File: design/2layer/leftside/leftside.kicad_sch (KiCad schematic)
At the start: 236 parts, among them IC2 MCP23009-E_MG, IC3 nRF52833-QDAA-R7, IC5 XCL110A503KR-G, IC6 TPS22917LDBVT, IC7 SN74AHCT1G125DCKR, IC8 TPS63051RMWT, J1 USB_C_Receptacle_USB2.0_16P, J2 Battery+, J3 Battery-, J4 OLED_128x32, J5 Conn_01x01, J6 Conn_01x04, J7 F32Q-1A7H1-11012, J8 Conn_01x01, U1 BQ27441-G1, U2 BQ24072RGT, U3 USB6B1, U5 PEC11L-4015F-S0015, Y1 ECS-320-8-37B2-JTY-TR

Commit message: Replaced TPS63051 with TPS63031 as out of stock
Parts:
- removed IC8: TPS63051RMWT, QFN50P250X250X100-12N-D, symbol SamacSys:TPS63051RMWT
- removed PG1: TestPoint, TestPoint:TestPoint_Pad_D1.0mm, symbol Connector:TestPoint
- added IC4: TPS63031DSKT, SON50P250X250X80-11N-D, symbol SamacSys:TPS63031DSKT
- PC1: value 10uF -> 100nF
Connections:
- net 3V3: now also PC3.2, PC47.2, IC4.1 (VOUT), IC4.10 (FB); no longer PC1.1, PC27.1
- net GND: now also PC1.1, PC27.1, PC3.1, PC47.1, IC4.11 (EP), IC4.3 (PGND), IC4.7 (PS/SYNC), IC4.9 (GND); no longer PC1.2, PC27.2, PC3.2, PC47.2
- net at IC5.1 (1/VIN), IC5.3 (3/EN), IC5.7 (7/L1)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: now also PC1.2, PC27.2, IC4.5 (VIN), IC4.6 (EN), IC4.8 (VINA); no longer PC3.1, PC47.1
- net at PL5.2: now also IC4.2 (L2)
- net at PL5.1: now also IC4.4 (L1)
- no-connect marks 18 -> 17
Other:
- moved on the sheet: IC5, PC25, PC26

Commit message: Create blender model + PCB review fixes
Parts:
- removed C29, C39, C4, C45: 100nF, ScottoKeebs_Components:Capacitor_0603, symbol Device:C_Small
- removed C44: 10uF, ScottoKeebs_Components:Capacitor_0603, symbol Device:C_Small
- removed PL5: 1.5uH, Inductor_SMD:L_0603_1608Metric, symbol Device:L_Small
- added C46, PC28: 100nF, ScottoKeebs_Components:Capacitor_0603, symbol Device:C_Small
- added PC29: 10uF, ScottoKeebs_Components:Capacitor_0603, symbol Device:C_Small
- added PL1: LPS3015-153MRC, Snapeda:IND_LPS3015-153MRC, symbol Device:L
- added SR17, SR18: 47, Resistor_SMD:R_0603_1608Metric, symbol Device:R
- added SR6: 100k, Resistor_SMD:R_0603_1608Metric, symbol Device:R
- C2, C21, C28, C3, C30, C31, C32, C33, C35, C36, C38, C41, C42, C43: value 100nF -> 10uF
- F1: value 6A -> .75A
- PR3: value 1k8 -> 2k2
- SC10: value 10nF -> 0nF(10)
- SR4: value 4k7 -> 100k
- renumbered PL4 to SL4
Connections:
- net 5V: now also C46.1, PC29.2
- net GND: now also C46.2, PC28.2, PC29.1, SR6.1
- net Row 0: now also Di1.2 (A), Di12.2 (A), Di16.2 (A), Di24.2 (A), Di7.2 (A); no longer Di1.1 (K), Di12.1 (K), Di16.1 (K), Di24.1 (K), Di7.1 (K)
- net Row 1: now also Di10.2 (A), Di2.2 (A), Di26.2 (A), Di8.2 (A), Di9.2 (A); no longer Di10.1 (K), Di2.1 (K), Di26.1 (K), Di8.1 (K), Di9.1 (K)
- net Row 2: now also Di13.2 (A), Di14.2 (A), Di15.2 (A), Di27.2 (A), Di3.2 (A); no longer Di13.1 (K), Di14.1 (K), Di15.1 (K), Di27.1 (K), Di3.1 (K)
- net Row 3: now also Di18.2 (A), Di19.2 (A), Di21.2 (A), Di28.2 (A), Di5.2 (A); no longer Di18.1 (K), Di19.1 (K), Di21.1 (K), Di28.1 (K), Di5.1 (K)
- net Row 4: now also Di17.2 (A), Di22.2 (A), Di23.2 (A), Di29.2 (A), Di6.2 (A); no longer Di17.1 (K), Di22.1 (K), Di23.1 (K), Di29.1 (K), Di6.1 (K)
- net Row 5: now also Di11.2 (A), Di20.2 (A), Di25.2 (A), Di30.2 (A), Di4.2 (A), IC2.9 (GP0); no longer Di11.1 (K), Di20.1 (K), Di25.1 (K), Di30.1 (K), Di4.1 (K), IC2.10 (GP1)
- net Row 6: now also Di36.2 (A), IC2.10 (GP1); no longer Di36.1 (K), IC2.11 (GP2)
- net SCL: now also SR17.2; no longer IC3.2 (P0.00)
- net SDA: now also SR18.2; no longer IC3.3 (P0.01)
- net VBUS: now also PC28.1
- net at S4.2: now also Di16.1 (K); no longer Di16.2 (A)
- net at S11.2: now also Di3.1 (K); no longer Di3.2 (A)
- net at IC4.5 (VIN), IC4.6 (EN), IC4.8 (VINA)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: no longer IC5.3 (3/EN)
- net at S22.2: now also Di6.1 (K); no longer Di6.2 (A)
- net at S6.2: now also Di8.1 (K); no longer Di8.2 (A)
- net at S23.2: now also Di22.1 (K); no longer Di22.2 (A)
- net at S19.2: now also Di19.1 (K); no longer Di19.2 (A)
- net at S8.2: now also Di2.1 (K); no longer Di2.2 (A)
- net at S2.2: now also Di7.1 (K); no longer Di7.2 (A)
- net at IC4.4 (L1): now also PL1.1
- net at IC4.2 (L2): now also PL1.2
- net at S17.2: now also Di18.1 (K); no longer Di18.2 (A)
- net at S26.2: now also Di11.1 (K); no longer Di11.2 (A)
- net at S35.2: now also Di36.1 (K); no longer Di36.2 (A)
- net at S29.2: now also Di25.1 (K); no longer Di25.2 (A)
- net at S14.2: now also Di15.1 (K); no longer Di15.2 (A)
- net at S13.2: now also Di14.1 (K); no longer Di14.2 (A)
- net at S24.2: now also Di23.1 (K); no longer Di23.2 (A)
- net at S3.2: now also Di12.1 (K); no longer Di12.2 (A)
- net at S28.2: now also Di20.1 (K); no longer Di20.2 (A)
- net at S9.2: now also Di10.1 (K); no longer Di10.2 (A)
- net at S30.2: now also Di30.1 (K); no longer Di30.2 (A)
- net at S1.2: now also Di1.1 (K); no longer Di1.2 (A)
- net at S10.2: now also Di26.1 (K); no longer Di26.2 (A)
- net at S12.2: now also Di13.1 (K); no longer Di13.2 (A)
- net at S25.2: now also Di29.1 (K); no longer Di29.2 (A)
- net at S18.2: now also Di5.1 (K); no longer Di5.2 (A)
- net at S5.2: now also Di24.1 (K); no longer Di24.2 (A)
- net at S7.2: now also Di9.1 (K); no longer Di9.2 (A)
- net at S20.2: now also Di28.1 (K); no longer Di28.2 (A)
- net at S27.2: now also Di4.1 (K); no longer Di4.2 (A)
- net at S15.2: now also Di27.1 (K); no longer Di27.2 (A)
- net at S21.2: now also Di17.1 (K); no longer Di17.2 (A)
- net at S16.2: now also Di21.1 (K); no longer Di21.2 (A)
- new net: IC3.3 (P0.01), SR18.1
- new net: IC3.2 (P0.00), SR17.1
- new net 5VEN: IC2.11 (GP2), IC5.3 (3/EN), SR6.2
- no-connect marks 17 -> 16
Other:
- note added: "Address: 0x55 (85)"
- note added: "BLE Enabled - QFN40 Config 5"
- note added: "Battery charging and USB power stage. ILIM controls input current limit calculated by 1550/R = limit. 3k = 500mA | 2k2 = 705mA ISET controls battery current charge limit calculated by 890/R = limit. 1.8k = 500mA | 1k = 890mA White LED for charging status with CHG. TPS2291 load switch for better stability when turning on/off. White LED for USB Power connection Optional film NTC thermistor for batt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"
- note removed: "BLE Enabled - QFN40 Config 3"
- note removed: "Battery charging and USB power stage. Output 3.3V. ILIM controls input current limit calculated by 1550/R = limit. 3k = 500mA | 1k8 = 860mA ISET controls battery current charge limit calculated by 890/R = limit. 1.8k = 500mA | 1k = 890mA White LED for charging status with CHG. TPS2291 load switch for better stability when turning on/off. White LED for USB Power connection Optional film NTC thermi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"
- moved on the sheet: Di1, Di10, Di11, Di12, Di13, Di14, Di15, Di16, Di17, Di18, Di19, Di2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

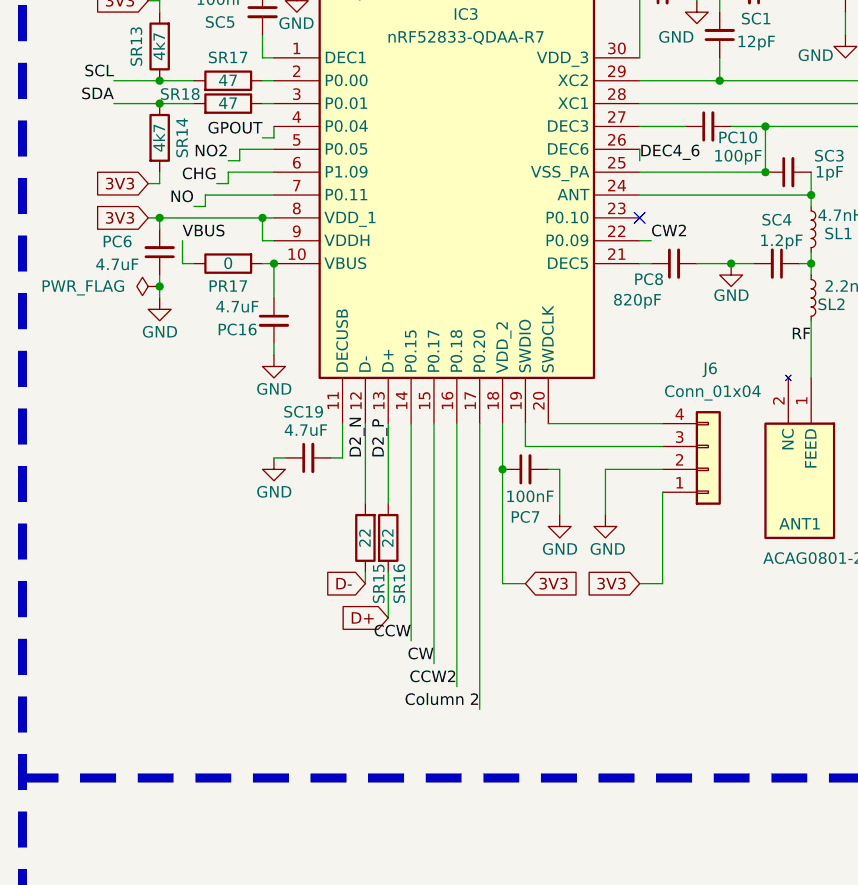
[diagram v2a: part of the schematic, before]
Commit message: Add keyboard render
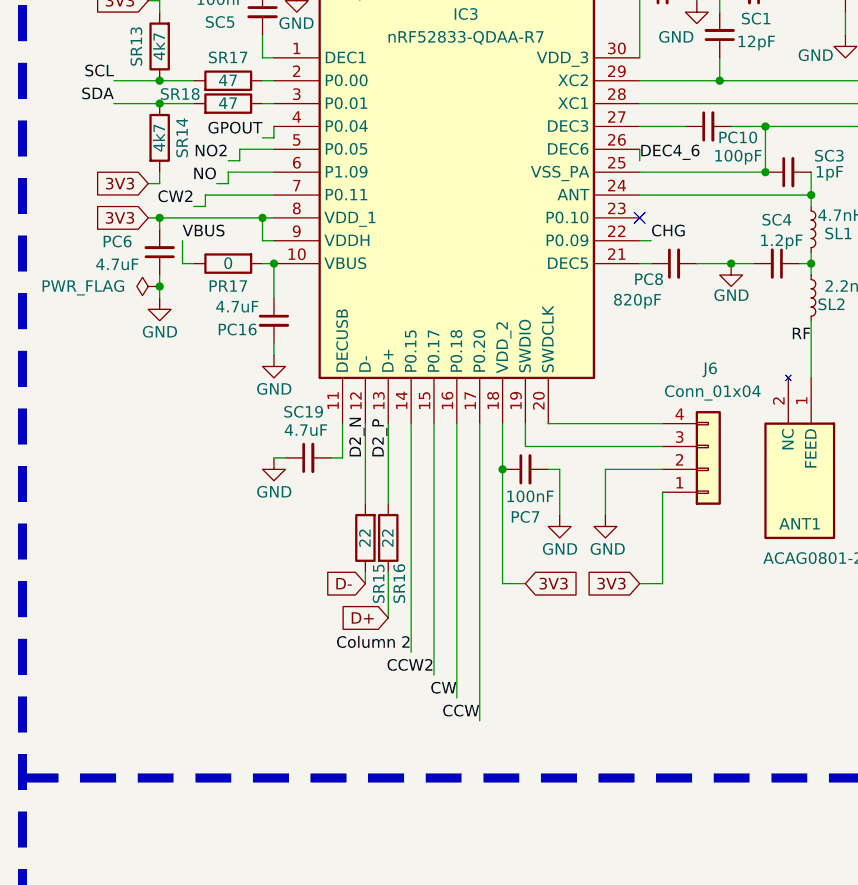
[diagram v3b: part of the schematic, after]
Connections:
- net CCW: now also IC3.17 (P0.20); no longer IC3.14 (P0.15)
- net CCW2: now also IC3.15 (P0.17); no longer IC3.16 (P0.18)
- net CHG: now also IC3.22 (P0.09); no longer IC3.6 (P1.09)
- net CW: now also IC3.16 (P0.18); no longer IC3.15 (P0.17)
- net CW2: now also IC3.7 (P0.11); no longer IC3.22 (P0.09)
- net Column 2: now also IC3.14 (P0.15); no longer IC3.17 (P0.20)
- net NO: now also IC3.6 (P1.09); no longer IC3.7 (P0.11)
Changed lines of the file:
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@@
 	(wire
 		(pts
-			(xy 59.69 124.46) (xy 59.69 151.13)
-		)
-		(stroke
-			(width 0)
-			(type default)
-		)
-	)
-	(wire
-		(pts
 			(xy 80.01 264.16) (xy 80.01 259.08)
 		)
@@
 	(wire
 		(pts
-			(xy 62.23 124.46) (xy 62.23 153.67)
-		)
-		(stroke
-			(width 0)
-			(type default)
-		)
-	)
-	(wire
-		(pts
 			(xy 554.99 137.16) (xy 551.18 137.16)
 		)
@@
 	(wire
 		(pts
-			(xy 64.77 124.46) (xy 64.77 156.21)
+			(xy 64.77 124.46) (xy 64.77 157.48)
 		)
 		(stroke
@@
 	(wire
 		(pts
-			(xy 57.15 124.46) (xy 57.15 148.59)
-		)
-		(stroke
-			(width 0)
-			(type default)
-		)
-	)
-	(wire
-		(pts
 			(xy 167.64 88.9) (xy 167.64 90.17)
 		)
@@
 	(wire
 		(pts
+			(xy 57.15 124.46) (xy 57.15 149.86)
+		)
+		(stroke
+			(width 0)
+			(type default)
+		)
+	)
+	(wire
+		(pts
 			(xy 483.87 35.56) (xy 506.73 35.56)
 		)
@@
 	(wire
 		(pts
+			(xy 62.23 124.46) (xy 62.23 154.94)
+		)
+		(stroke
+			(width 0)
+			(type default)
+		)
+	)
+	(wire
+		(pts
 			(xy 39.37 198.12) (xy 39.37 196.85)
 		)
@@
 	(wire
 		(pts
+			(xy 59.69 124.46) (xy 59.69 152.4)
+		)
+		(stroke
+			(width 0)
+			(type default)
+		)
+	)
+	(wire
+		(pts
 			(xy 430.53 172.72) (xy 430.53 198.12)
 		)
@@
 	)
 	(label "CCW2"
-		(at 62.23 153.67 180)
+		(at 59.69 152.4 180)
 		(effects
 			(font
@@
 	)
 	(label "CCW"
-		(at 57.15 148.59 180)
+		(at 64.77 157.48 180)
 		(effects
 			(font
@@
 	)
 	(label "CHG"
-		(at 35.56 97.79 180)
+		(at 83.82 104.14 0)
 		(effects
 			(font
 				(size 1.27 1.27)
 			)
-			(justify right bottom)
+			(justify left bottom)
 		)
 	)
@@
 	)
 	(label "Column 2"
-		(at 64.77 156.21 180)
+		(at 57.15 149.86 180)
 		(effects
 			(font
@@
 	)
 	(label "CW2"
-		(at 83.82 104.14 0)
+		(at 33.02 100.33 180)
 		(effects
 			(font
 				(size 1.27 1.27)
 			)
-			(justify left bottom)
+			(justify right bottom)
 		)
 	)
@@
 	)
 	(label "CW"
-		(at 59.69 151.13 180)
+		(at 62.23 154.94 180)
 		(effects
 			(font
@@
 	)
 	(label "NO"
-		(at 33.02 100.33 180)
+		(at 35.56 97.79 180)
 		(effects
 			(font
